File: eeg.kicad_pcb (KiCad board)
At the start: 2 copper layers, 81.4 x 54.9 mm, 133 parts, among them J1 Conn_01x05_Male, J10 USB_B_Mini, J2 Conn_01x05_Male, J3 Conn_01x05_Male, J4 Conn_01x05_Male, J5 Conn_01x10, J6 Conn_01x10_Male, J7 Conn_01x10_Male, SW3 EVQ-Q2K03W, U1 STM32F446RE, U12 RN4678-V_RM100, U2 ADS1299-8CHANNEL, U3 LD39050PU33R, U4 TPS60403DBVT, U5 TPS73225DBVT, U6 TPS72325DBVT, Y1 16.00Mhz

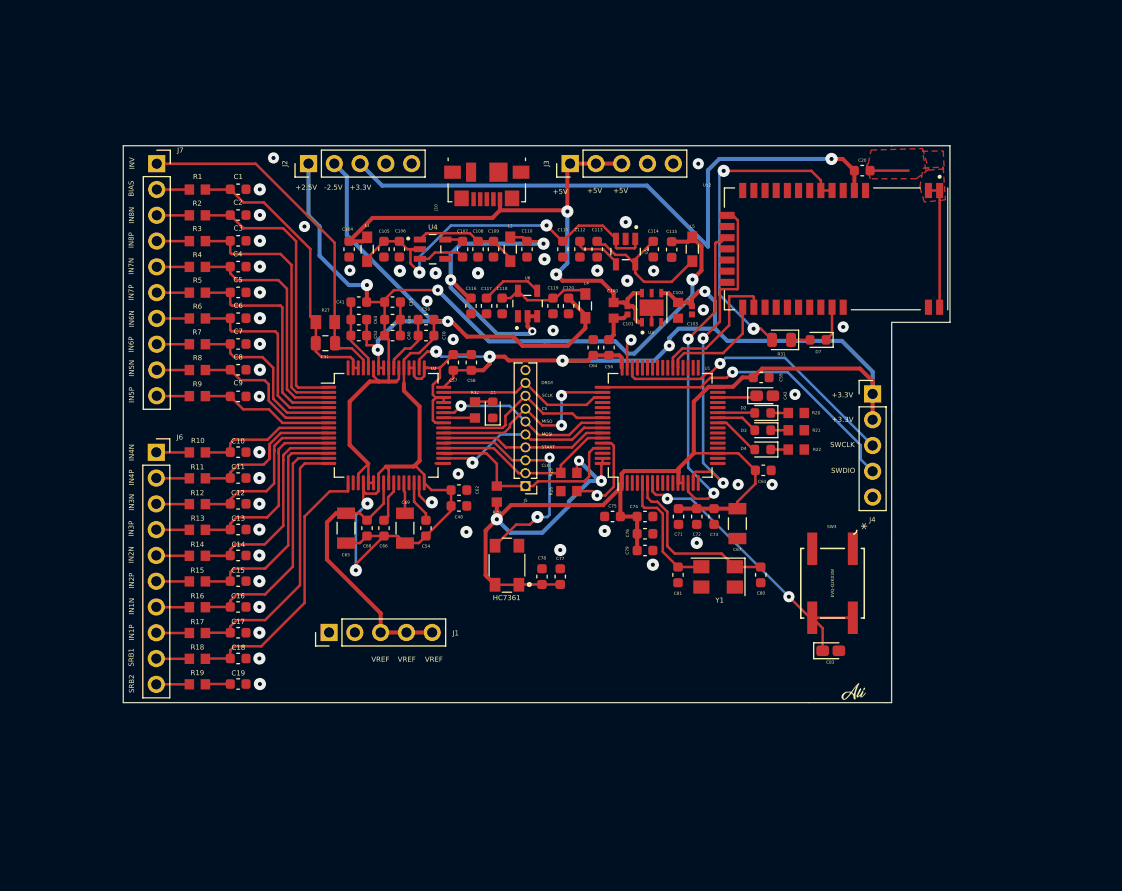
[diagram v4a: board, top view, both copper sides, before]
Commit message: vias changed to pad
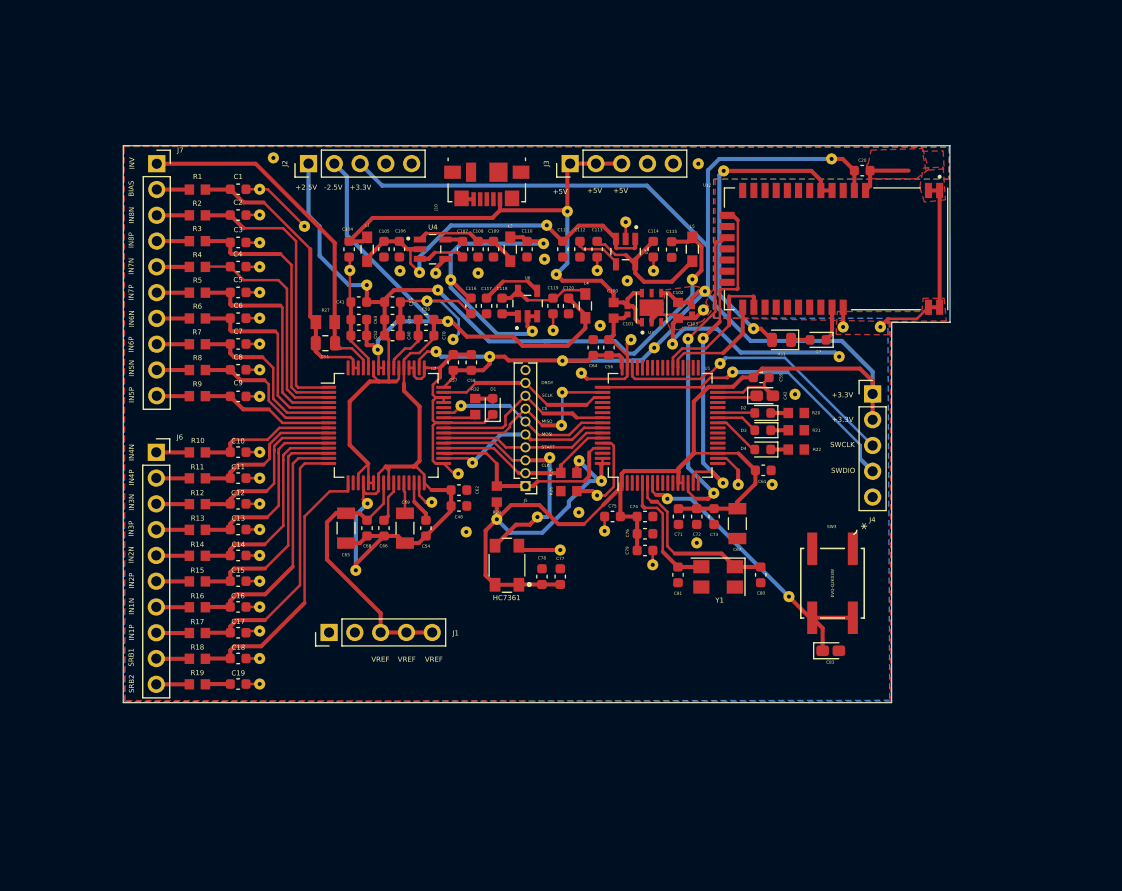
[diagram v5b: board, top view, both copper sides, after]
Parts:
- removed G***: LOGO, ali1:ali1
- added REF**: via1.11, ali1:via1.11, F.Cu at (97.2, 32.5)
- added REF**: via1.11, ali1:via1.11, F.Cu at (97.2, 63.2)
- added REF**: via1.11, ali1:via1.11, F.Cu at (96.3, 64.2)
- added REF**: via1.11, ali1:via1.11, F.Cu at (91.7, 64.8)
- added REF**: via1.11, ali1:via1.11, F.Cu at (78.9, 66.5)
- added REF**: via1.11, ali1:via1.11, F.Cu at (84.8, 64.4)
- added REF**: via1.11, ali1:via1.11, F.Cu at (71.4, 55.6)
- added REF**: via1.11, ali1:via1.11, F.Cu at (72.5, 61.2)
- added REF**: via1.11, ali1:via1.11, F.Cu at (80.1, 60.7)
- added REF**: via1.11, ali1:via1.11, F.Cu at (81.3, 57.5)
- added REF**: via1.11, ali1:via1.11, F.Cu at (81.3, 54.3)
- added REF**: via1.11, ali1:via1.11, F.Cu at (79.8, 37.8)
- added REF**: via1.11, ali1:via1.11, F.Cu at (85.2, 63.0)
- added REF**: via1.11, ali1:via1.11, F.Cu at (83.0, 61.0)
- added REF**: via1.11, ali1:via1.11, F.Cu at (81.8, 36.4)
- added REF**: via1.11, ali1:via1.11, F.Cu at (80.8, 42.6)
- added REF**: via1.11, ali1:via1.11, F.Cu at (61.0, 71.8)
- added REF**: via1.11, ali1:via1.11, F.Cu at (62.1, 65.2)
- added REF**: via1.11, ali1:via1.11, F.Cu at (70.1, 47.3)
- added REF**: via1.11, ali1:via1.11, F.Cu at (63.2, 50.1)
- added REF**: via1.11, ali1:via1.11, F.Cu at (84.8, 42.3)
- added REF**: via1.11, ali1:via1.11, F.Cu at (79.5, 39.6)
- added REF**: via1.11, ali1:via1.11, F.Cu at (56.0, 37.9)
- added REF**: via1.11, ali1:via1.11, F.Cu at (78.4, 48.2)
- added REF**: via1.11, ali1:via1.11, F.Cu at (107.9, 31.3)
- added REF**: via1.11, ali1:via1.11, F.Cu at (74.9, 66.8)
- added REF**: via1.11, ali1:via1.11, F.Cu at (68.9, 50.2)
- added REF**: via1.11, ali1:via1.11, F.Cu at (74.2, 50.8)
- added REF**: via1.11, ali1:via1.11, F.Cu at (81.4, 51.2)
- added REF**: via1.11, ali1:via1.11, F.Cu at (90.4, 49.9)
- added REF**: via1.11, ali1:via1.11, F.Cu at (95.4, 44.3)
- added REF**: via1.11, ali1:via1.11, F.Cu at (94.2, 43.1)
- added REF**: via1.11, ali1:via1.11, F.Cu at (62.1, 43.7)
- added REF**: via1.11, ali1:via1.11, F.Cu at (103.7, 74.4)
- added REF**: via1.11, ali1:via1.11, F.Cu at (69.1, 44.2)
- added REF**: via1.11, ali1:via1.11, F.Cu at (70.4, 43.2)
- added REF**: via1.11, ali1:via1.11, F.Cu at (67.3, 42.5)
- added REF**: via1.11, ali1:via1.11, F.Cu at (83.2, 52.4)
- added REF**: via1.11, ali1:via1.11, F.Cu at (83.0, 66.1)
- added REF**: via1.11, ali1:via1.11, F.Cu at (81.2, 69.8)
- added REF**: via1.11, ali1:via1.11, F.Cu at (85.5, 67.9)
- added REF**: via1.11, ali1:via1.11, F.Cu at (90.3, 71.3)
- added REF**: via1.11, ali1:via1.11, F.Cu at (94.6, 69.1)
- added REF**: via1.11, ali1:via1.11, F.Cu at (98.7, 63.4)
- added REF**: via1.11, ali1:via1.11, F.Cu at (100.2, 48.0)
- added REF**: via1.11, ali1:via1.11, F.Cu at (102.0, 63.4)
- added REF**: via1.11, ali1:via1.11, F.Cu at (95.2, 46.1)
- added REF**: via1.11, ali1:via1.11, F.Cu at (90.3, 42.3)
- added REF**: via1.11, ali1:via1.11, F.Cu at (87.8, 43.3)
- added REF**: via1.11, ali1:via1.11, F.Cu at (94.8, 31.8)
- added REF**: via1.11, ali1:via1.11, F.Cu at (112.7, 47.8)
- added REF**: via1.11, ali1:via1.11, F.Cu at (109.0, 47.8)
- added REF**: via1.11, ali1:via1.11, F.Cu at (108.6, 50.8)
- added REF**: via1.11, ali1:via1.11, F.Cu at (104.3, 54.5)
- added REF**: via1.11, ali1:via1.11, F.Cu at (92.2, 49.5)
- added REF**: via1.11, ali1:via1.11, F.Cu at (98.1, 52.3)
- added REF**: via1.11, ali1:via1.11, F.Cu at (88.1, 49.1)
- added REF**: via1.11, ali1:via1.11, F.Cu at (85.1, 47.7)
- added REF**: via1.11, ali1:via1.11, F.Cu at (80.5, 48.2)
- added REF**: via1.11, ali1:via1.11, F.Cu at (73.1, 42.5)
- added REF**: via1.11, ali1:via1.11, F.Cu at (79.6, 41.1)
- added REF**: via1.11, ali1:via1.11, F.Cu at (87.6, 37.5)
- added REF**: via1.11, ali1:via1.11, F.Cu at (52.9, 31.2)
- added REF**: via1.11, ali1:via1.11, F.Cu at (51.5, 39.5)
- added REF**: via1.11, ali1:via1.11, F.Cu at (51.5, 41.9)
- added REF**: via1.11, ali1:via1.11, F.Cu at (51.5, 62.7)
- added REF**: via1.11, ali1:via1.11, F.Cu at (96.9, 51.4)
- added REF**: via1.11, ali1:via1.11, F.Cu at (60.4, 42.2)
- added REF**: via1.11, ali1:via1.11, F.Cu at (65.4, 42.3)
- added REF**: via1.11, ali1:via1.11, F.Cu at (68.9, 42.5)
- added REF**: via1.11, ali1:via1.11, F.Cu at (68.0, 45.3)
- added REF**: via1.11, ali1:via1.11, F.Cu at (70.6, 49.0)
- added REF**: via1.11, ali1:via1.11, F.Cu at (71.1, 62.3)
- added REF**: via1.11, ali1:via1.11, F.Cu at (68.5, 65.1)
- added REF**: via1.11, ali1:via1.11, F.Cu at (71.9, 68.0)
- added REF**: via1.11, ali1:via1.11, F.Cu at (51.5, 47.0)
- added REF**: via1.11, ali1:via1.11, F.Cu at (51.5, 83.0)
- added REF**: via1.11, ali1:via1.11, F.Cu at (93.7, 49.0)
- added REF**: via1.11, ali1:via1.11, F.Cu at (51.5, 80.5)
- added REF**: via1.11, ali1:via1.11, F.Cu at (51.5, 77.8)
- added REF**: via1.11, ali1:via1.11, F.Cu at (51.5, 75.4)
- added REF**: via1.11, ali1:via1.11, F.Cu at (51.5, 72.9)
- added REF**: via1.11, ali1:via1.11, F.Cu at (51.5, 70.3)
- added REF**: via1.11, ali1:via1.11, F.Cu at (51.5, 67.8)
- added REF**: via1.11, ali1:via1.11, F.Cu at (51.5, 65.3)
- added REF**: via1.11, ali1:via1.11, F.Cu at (51.5, 60.2)
- added REF**: via1.11, ali1:via1.11, F.Cu at (51.5, 54.7)
- added REF**: via1.11, ali1:via1.11, F.Cu at (51.5, 52.0)
- added REF**: via1.11, ali1:via1.11, F.Cu at (95.2, 49.0)
- added REF**: via1.11, ali1:via1.11, F.Cu at (51.5, 49.5)
- added REF**: via1.11, ali1:via1.11, F.Cu at (51.5, 44.4)
- added REF**: via1.11, ali1:via1.11, F.Cu at (51.5, 36.8)
- added REF**: via1.11, ali1:via1.11, F.Cu at (51.5, 34.3)
- moved D1 0.35 mm to (74.5, 55.6)
- moved R32 0.33 mm to (72.8, 55.7)
- moved C3 0.16 mm to (49.4, 39.5)
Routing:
- net GNDA: track 59.5 -> 196.7 mm, vias 47 -> 0
- net +3V3: track 255.8 -> 262.0 mm, vias 9 -> 0
- net +5V: track 56.8 -> 56.4 mm, vias 2 -> 0
- net CS: track 20.6 -> 20.7 mm, vias 2 -> 0
- net SWDIO: vias 1 -> 0
- net SWCLK: vias 1 -> 0
- net Net-(R31-Pad2): vias 2 -> 0
- net Net-(R26-Pad2): vias 1 -> 0
- net Net-(C83-Pad1): vias 2 -> 0
- net Net-(C105-Pad1): vias 2 -> 0
- net MOSI: vias 1 -> 0
- net MISO: vias 1 -> 0
- net /RN46RTS: vias 2 -> 0
- net /RN46CTS: vias 2 -> 0
- net /CLK: vias 2 -> 0
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- added copper zone on B.Cu, net GNDA
